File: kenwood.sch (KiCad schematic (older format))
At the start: 14 parts, among them IC1 ATMEGA168A-A, Q1 CRYSTAL, SW1 SPST, U1 TL7705

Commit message: Switching to atmega164, muxing the two seven-segs instead of using IO exapander.
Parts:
- removed IC1: ATMEGA168A-A, TQFP32, symbol ATMEGA168A-A
- added IC?: ATMEGA164PA-A, TQFP44, symbol ATMEGA164PA-A
- added LDD?: LDD-A812RI, symbol LDD-A812RI
- added P?: CONN_2, symbol CONN_2
- added Q? (x2): MOSFET_N, symbol MOSFET_N
- added R?: 10K, symbol R
- added RP?: R_PACK8, symbol R_PACK8
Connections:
- net labels added: LED_A, LED_B, LED_C, LED_D, LED_DP, LED_E, LED_F, LED_G, RX, SCL, SDA, TX
- net labels removed: CFG_BUTTON
- wire segments 61 -> 65
- no-connect marks 2 -> 0
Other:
- moved on the sheet: C1, C2, C3, C4, ICSP1, R1, R2, R3, R4, SERIAL1, U1

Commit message: First experiments with board layout, plus modules for the AC/DC power unit and LCD.
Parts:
- removed Q? (x2): MOSFET_N, symbol MOSFET_N
- removed RP?: R_PACK8, symbol R_PACK8
- added Q3: DUAL_MOS_P, symbol DUAL_MOS_P
- added R14, R15: 10K, symbol R
- gave numbers to parts that had none: 4
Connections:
- net labels added: SEG_0, SEG_1
- wire segments 65 -> 43
- no-connect marks 0 -> 4
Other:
- moved on the sheet: LDD1

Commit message: Adding back library files in same repo.
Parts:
- removed P1: CONN_2, symbol CONN_2
- removed R14, R15: 10K, symbol R
- removed SW1: SPST, symbol SPST
- added C15: 0.2u, symbol CP1
- added ENC1: PEC11L, MODULE, symbol PEC11L
- added P6, P7, P8, P9: CONN_1, symbol CONN_1
- added U7: TSOP382, SIP3, symbol TSOP382
- R13: value 10K -> 100
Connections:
- net labels added: BTN_IN, MUX_A, MUX_B, ~SCE
- wire segments 43 -> 63

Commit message: Changing dual fet module.
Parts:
- removed Q3: DUAL_MOS_P, symbol DUAL_MOS_P
- added C5, C6, C7, C8: C, symbol C
- added U2: DMP2066LSD, MODULE, symbol DMP2066LSD
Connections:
- wire segments 63 -> 71

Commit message: Moving back to atmega168, for cost and size reduction, new smaller board layout.
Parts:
- removed C1, C2: 22P, symbol C
- removed C6, C7, C8: C, symbol C
- removed IC1: ATMEGA164PA-A, TQFP44, symbol ATMEGA164PA-A
- removed Q1: CRYSTAL, symbol CRYSTAL
- added D1: LED, symbol LED
- added IC1: ATMEGA168-A, TQFP32, symbol ATMEGA168-A
- added R5: 100, symbol R
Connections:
- net labels added: ENC_A, ENC_B, MONITOR_L, MONITOR_R, RELAY
- net labels removed: AMP_ENABLE, VOL_ENC_A, VOL_ENC_B, XTAL1, XTAL2, ~SCE
- wire segments 71 -> 72
- no-connect marks 4 -> 0
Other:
- moved on the sheet: C15, C4, C5, ENC1, ICSP1, LDD1, R1, R13, R2, R3, R4, U1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

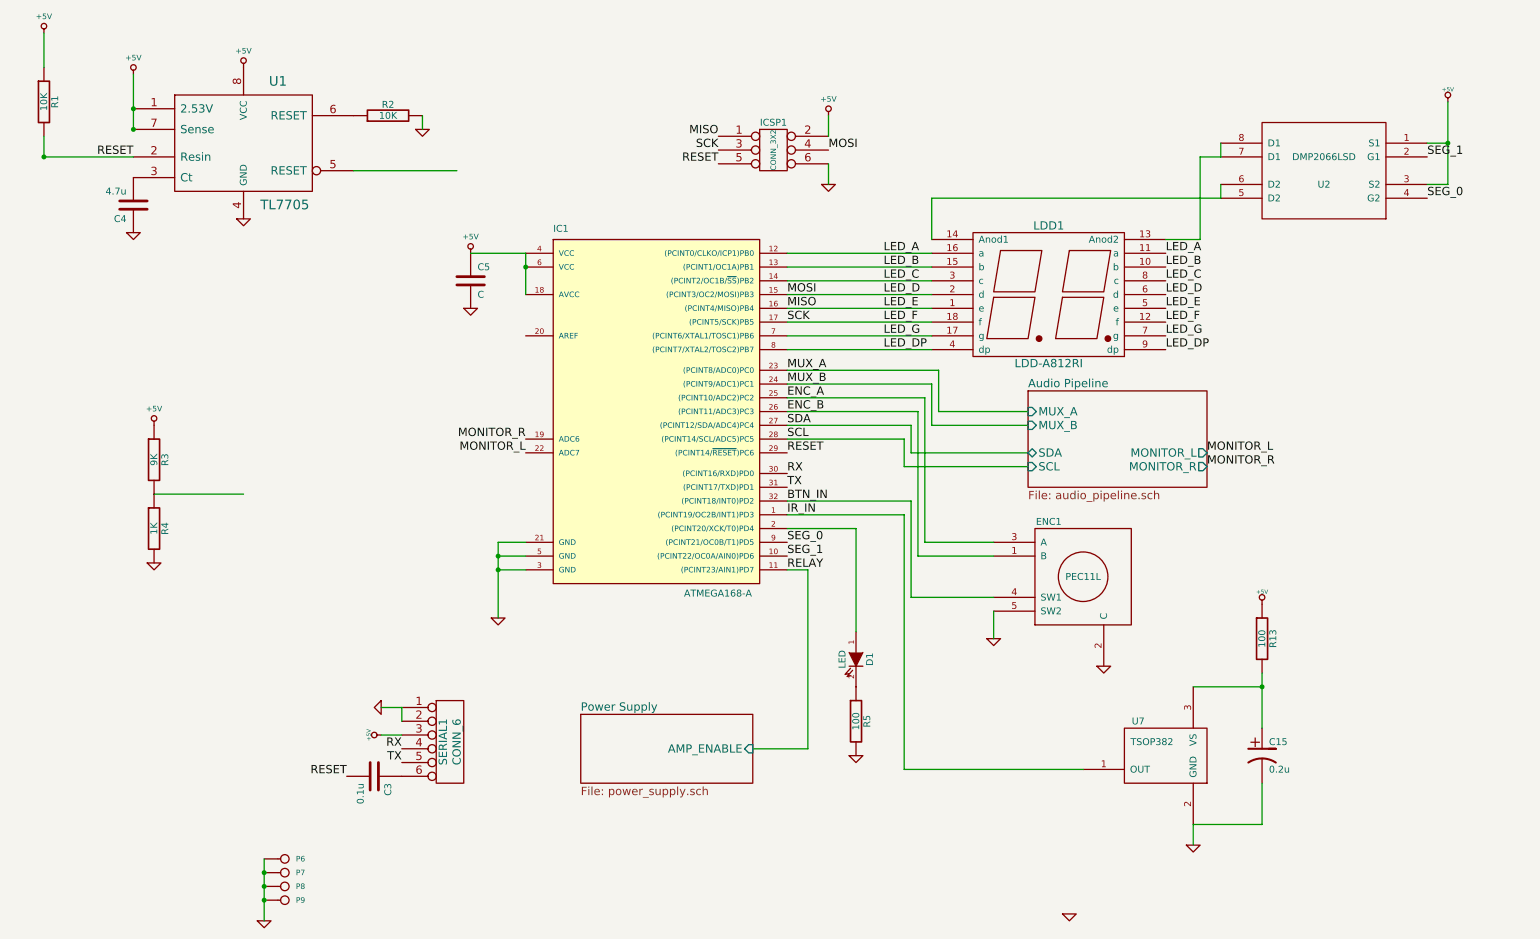
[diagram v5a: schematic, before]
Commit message: Removing reset circuit, finishing audio circuit.
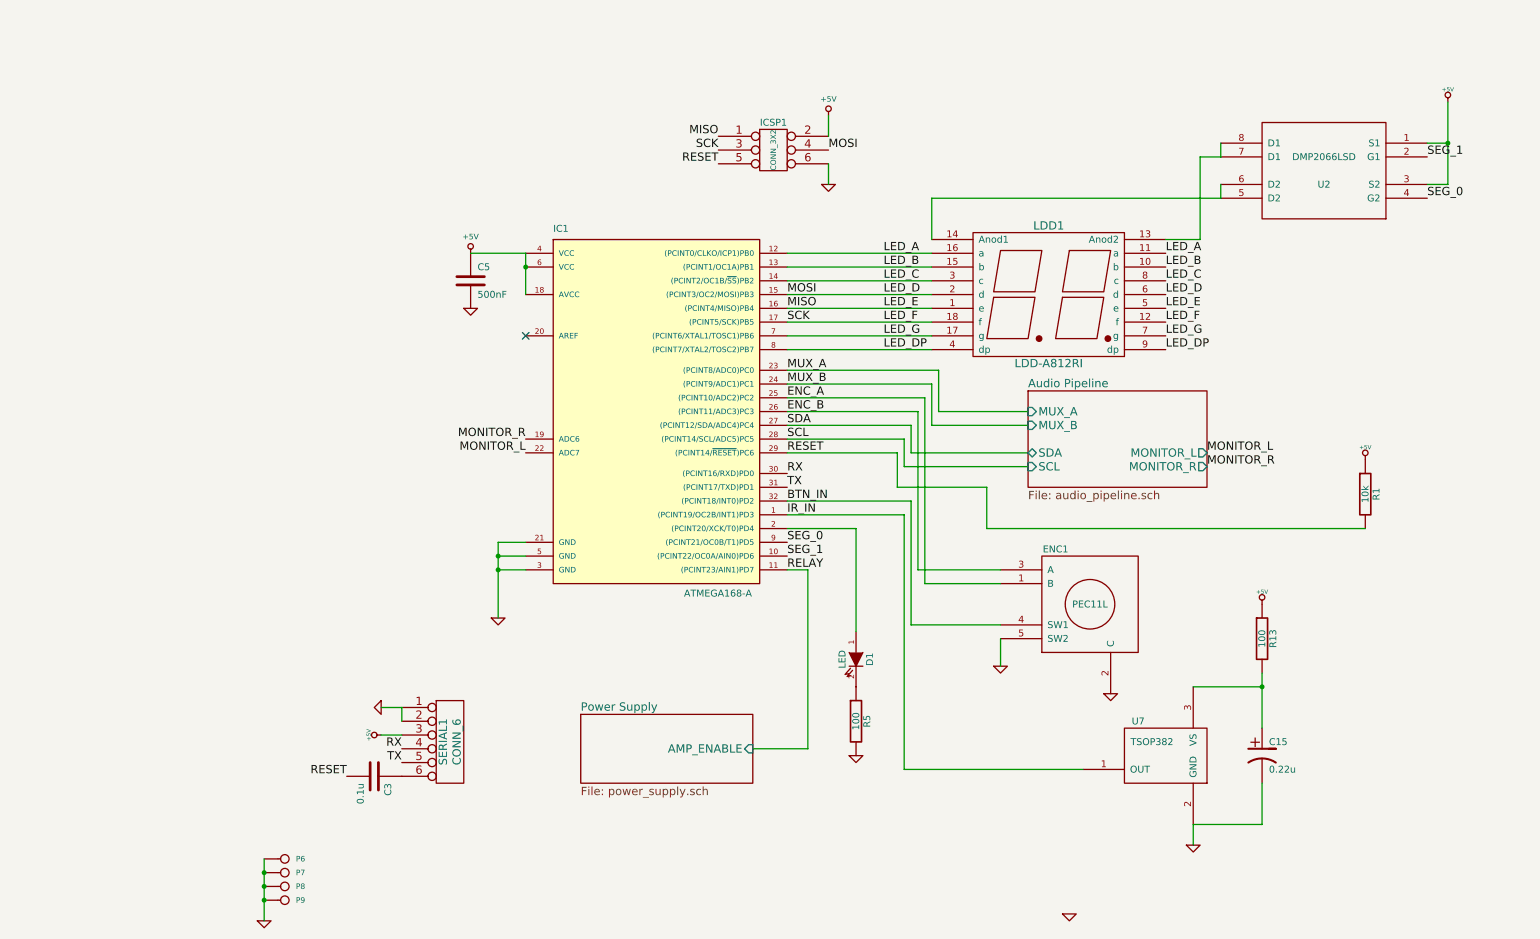
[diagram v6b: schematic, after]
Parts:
- removed C4: 4.7u, symbol C
- removed R2: 10K, symbol R
- removed R3: 9K, symbol R
- removed R4: 1K, symbol R
- removed U1: TL7705, symbol TL7705
- C15: value 0.2u -> 0.22u
- C5: value C -> 500nF
- R1: value 10K -> 10k
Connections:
- net ENC_A: now also ENC1.1 (B); no longer ENC1.3 (A)
- net ENC_B: now also ENC1.3 (A); no longer ENC1.1 (B)
- no-connect marks 0 -> 1
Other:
- moved on the sheet: ENC1

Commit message: Final touches on a rev0.0 candidate.
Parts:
- removed P9: CONN_1, symbol CONN_1
- C5: value 500nF -> 500n
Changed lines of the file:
@@
-EESchema Schematic File Version 2  date 8/1/2012 4:30:13 PM
+EESchema Schematic File Version 2  date 8/1/2012 10:55:27 PM
 LIBS:atmel
 LIBS:device
@@
 LIBS:RC4580
 LIBS:DMP2066LSD
+LIBS:MAX660
 LIBS:kenwood-cache
 EELAYER 25  0
@@
 Sheet 1 3
 Title ""
-Date "1 aug 2012"
+Date "2 aug 2012"
 Rev ""
 Comp ""
@@
 Wire Wire Line
 	8950 5350 9450 5350
-Connection ~ 2200 6900
 Wire Wire Line
 	10650 1400 10800 1400
@@
 P 3700 2400
 F 0 "C5" H 3750 2500 50  0000 L CNN
-F 1 "500nF" H 3750 2300 50  0000 L CNN
+F 1 "500n" H 3750 2300 50  0000 L CNN
 	1    3700 2400
 	1    0    0    -1
@@
 F 1 "GND" H 2200 7075 40  0001 C CNN
 	1    2200 7050
-	1    0    0    -1
-$EndComp
-$Comp
-L CONN_1 P9
-U 1 1 5011FA13
-P 2350 6900
-F 0 "P9" H 2430 6900 40  0000 L CNN
-F 1 "CONN_1" H 2350 6955 30  0001 C CNN
-	1    2350 6900
 	1    0    0    -1
 $EndComp
@@
 RESET
 $Comp
-L +5V #PWR014
+L +5V #PWR013
 U 1 1 4F897B54
 P 3050 5700
-F 0 "#PWR014" H 3050 5790 20  0001 C CNN
+F 0 "#PWR013" H 3050 5790 20  0001 C CNN
 F 1 "+5V" H 3050 5790 30  0000 C CNN
 	1    3050 5700
@@
 $EndComp
 $Comp
-L +5V #PWR015
+L +5V #PWR014
 U 1 1 4F84C247
 P 3700 2200
-F 0 "#PWR015" H 3700 2350 40  0001 C CNN
+F 0 "#PWR014" H 3700 2350 40  0001 C CNN
 F 1 "+5V" H 3700 2320 40  0000 C CNN
 	1    3700 2200
@@
 $EndComp
 $Comp
-L +5V #PWR016
+L +5V #PWR015
 U 1 1 4F8254DC
 P 6300 1200
-F 0 "#PWR016" H 6300 1350 40  0001 C CNN
+F 0 "#PWR015" H 6300 1350 40  0001 C CNN
 F 1 "+5V" H 6300 1320 40  0000 C CNN
 	1    6300 1200
@@
 $EndComp
 $Comp
-L GND #PWR017
+L GND #PWR016
 U 1 1 4F8254C1
 P 6300 1700
-F 0 "#PWR017" H 6300 1775 40  0001 C CNN
+F 0 "#PWR016" H 6300 1775 40  0001 C CNN
 F 1 "GND" H 6300 1725 40  0001 C CNN
 	1    6300 1700

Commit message: Final board as sent for fab.
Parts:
- removed R1: 10k, symbol R
- added RP1: 6.8k, symbol R_PACK4
- added U4: MC33064D, symbol MC33064D
- C15: value 0.22u -> 0.68u
- C5: value 500n -> 0.68u
- R5: value 100 -> 330
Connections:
- net +5V: now also RP1.1 (P1), RP1.2 (P2), RP1.3 (P3), RP1.4 (P4), U4.2 (In)
- net GND: now also U4.4 (Gnd)
- net RESET: now also RP1.7 (R2), U4.1 (RST)
- net SCL: now also RP1.6 (R3)
- net SDA: now also RP1.5 (R4)
- net RELAY renamed AMP_ENABLE
- net AMP_ENABLE: now also RP1.8 (R1)
